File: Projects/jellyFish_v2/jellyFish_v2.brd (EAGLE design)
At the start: 160 x 90 mm, 42 parts, among them P1 50, P2 50, P3 50, P4 50, P5 100, P6 100, P7 100, P8 100, Q1 IRF520, Q2 IRF520, Q3 IRF520, Q4 IRF520

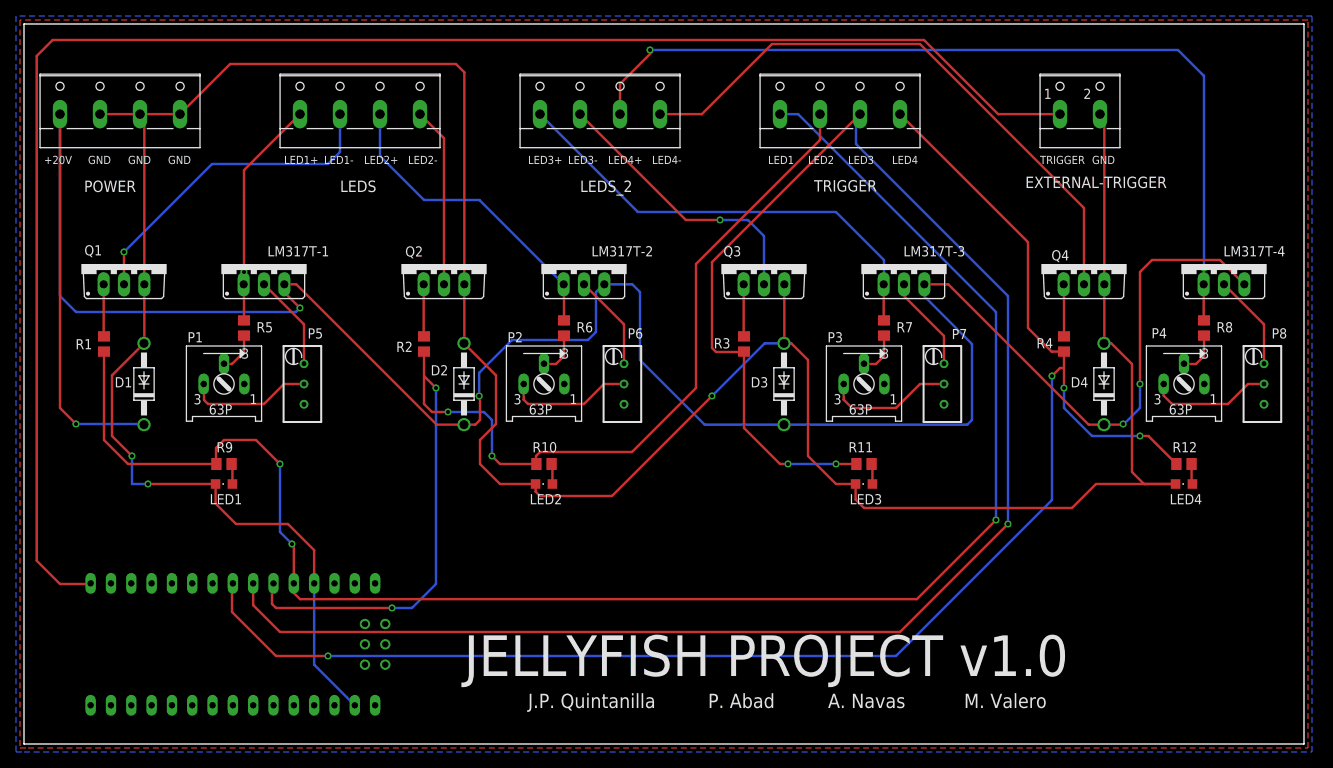
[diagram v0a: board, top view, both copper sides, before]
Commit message: Added Trigger Outputs
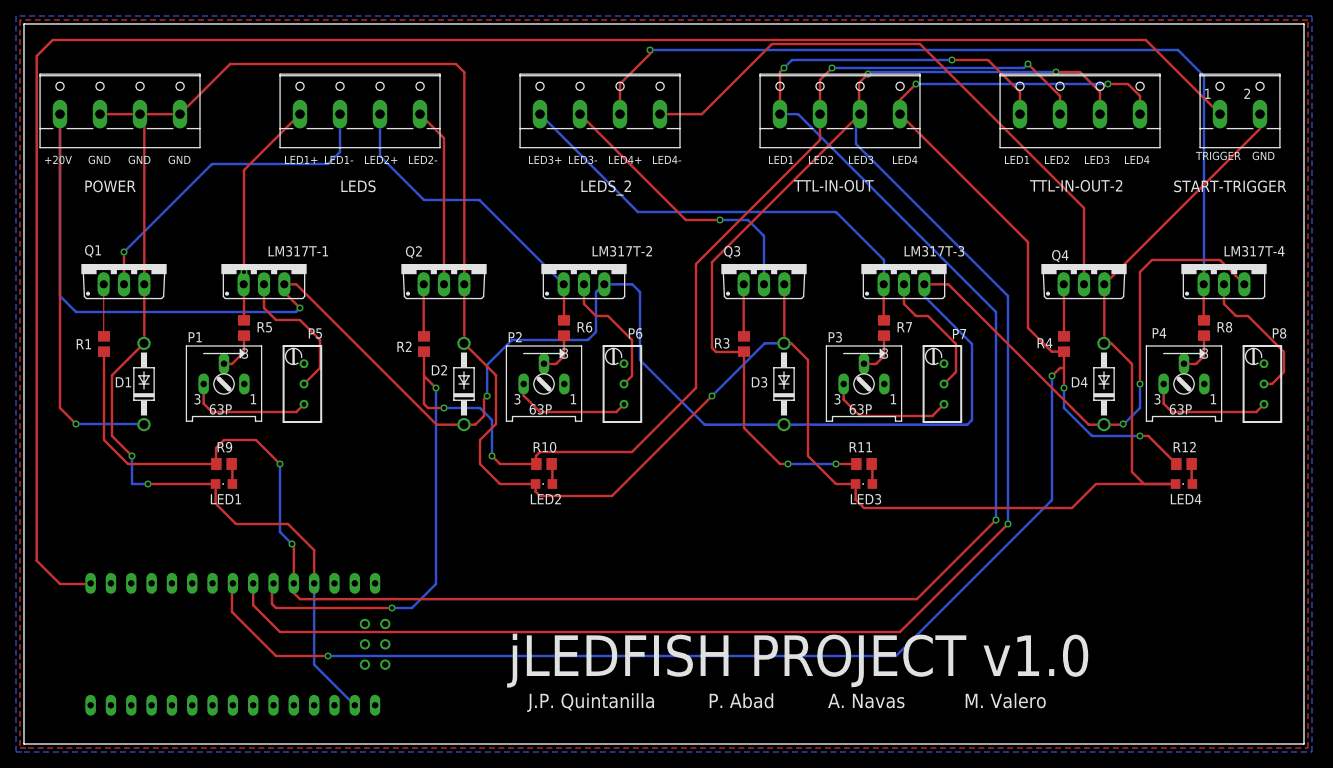
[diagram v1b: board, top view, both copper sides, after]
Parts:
- removed EXTERNAL-TRIGGER: (no value), con-wago-500:W237-102
- added START-TRIGGER: (no value), con-wago-500:W237-102
- added TTL-IN-OUT-2: (no value), con-wago-500:W237-4
- renumbered TRIGGER to TTL-IN-OUT
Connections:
- net GND: now also START-TRIGGER.2; no longer EXTERNAL-TRIGGER.2
- net N$1: now also P7.1; no longer P7.2
- net N$10: now also TTL-IN-OUT-2.3
- net N$12: now also P4.E, P8.1; no longer LM317T-3.2, P7.3
- net N$14: now also LM317T-3.2, P7.2; no longer P4.E, P8.2
- net N$15: now also P5.1; no longer P5.2
- net N$18: now also P6.2; no longer P6.3
- net N$21: now also START-TRIGGER.1; no longer EXTERNAL-TRIGGER.1
- net N$23: now also TTL-IN-OUT-2.4
- net N$26: now also P8.2; no longer P8.3
- net N$27: now also P5.2; no longer P5.3
- net N$3: now also TTL-IN-OUT-2.1
- net N$5: now also P6.1; no longer P6.2
- net N$6: now also TTL-IN-OUT-2.2
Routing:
- net N$3: track 210.3 -> 250.6 mm, vias 3 -> 5
- net N$6: track 142.8 -> 181.8 mm, vias 4 -> 6
- net N$10: track 229.9 -> 268.6 mm, vias 3 -> 5
- net N$23: track 197.0 -> 232.5 mm, vias 4 -> 6
- net N$21: track 203.6 -> 223.6 mm
- net GND: track 373.7 -> 381.6 mm
- net N$26: track 12.0 -> 18.1 mm
- net N$27: track 12.0 -> 17.9 mm
- net N$18: track 12.0 -> 16.2 mm
- net N$12: track 12.0 -> 15.8 mm
- net N$14: track 15.5 -> 16.7 mm
- net N$5: track 15.8 -> 15.2 mm
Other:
- board text added: "jLEDFISH PROJECT v1.0"
- board text removed: "JELLYFISH PROJECT v1.0"
